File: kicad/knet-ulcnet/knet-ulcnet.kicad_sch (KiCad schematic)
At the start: 16 parts, among them U1 74LS157, U2 74LS00, U3 74LS139, U4 74LS86, U5 74LS74, U6 74LS74, U7 74LS123, U8 SN75176AP, U9 LM339

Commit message: Update schematics etc for WEB-NT product
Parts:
- added C*, C4: 103, symbol Device:C
- added C1: 10/35, symbol Device:C_Polarized
- added C2: 270p, symbol Device:C
- added C3: 470p, symbol Device:C
- added J1: EXT, symbol Connector_Generic:Conn_01x06
- added Q1: 2N2222A, symbol Device:Q_NPN_BCE
- added R10, R11: 10M, symbol Device:R
- added R12, R9: 22K, symbol Device:R
- added R2: 12K, symbol Device:R
- added R3: 47K, symbol Device:R
- added R4: 6.8K, symbol Device:R
- added R5: 120, symbol Device:R
- added R6: 3.9K1%, symbol Device:R
- added R7: 1.5K1%, symbol Device:R
- added R8: 4.7K, symbol Device:R
- ?: value SIO0-DIP-40 -> (none); Value_1 SIO0-DIP-40 -> (Z80A-SIO/0)
- D1, D2: renamed from D?; value (none) -> 5.6V
- D3, D4: renamed from D?; value D -> (none)
- J2: renamed from J?; value Conn_01x04 -> NET
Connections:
- net GND: now also U1.15 (E), U1.8 (GND), U2.7 (GND), U3.13 (A1), U3.8 (GND), U4.7 (GND), U5.7 (GND), U6.7 (GND), U7.1 (A), U7.8 (GND), U7.9 (A), U9.12 (V-), C*.2, C1.2, C4.2, J1.5 (Pin_5), Q1.3 (E), R7.2; no longer D3.2 (A), D4.2 (A), U8.5 (GND)
- net VCC: now also U1.16 (VCC), U2.13, U2.14 (VCC), U3.16 (VCC), U4.10, U4.13, U4.14 (VCC), U5.1 (~{R}), U5.10 (~{S}), U5.14 (VCC), U5.4 (~{S}), U6.1 (~{R}), U6.10 (~{S}), U6.14 (VCC), U6.4 (~{S}), U7.11 (Clr), U7.16 (VCC), U7.3 (Clr), U8.8 (VCC), U9.3 (V+), C*.1, C1.1, J1.4 (Pin_4), R2.1, R3.1, R5.2, R6.1, R8.1
- net NET: now reaches U1.1 (S), U2.10, U2.11, U3.2 (A0)
- net NET: now also U3.14 (A0)
- net 500KHz: now reaches U1.10 (I1c)
- net 500KHz: now also U4.4, U5.9 (Q)
- net 14: now reaches U1.11 (I0c)
- net /CTS: now reaches U1.12 (Zd)
- net /CTS: now also ?.18 (~{CTSA})
- net at U1.13 (I1d): now also U6.5 (Q)
- net 18: now reaches U1.14 (I0d)
- net 12: now reaches U1.2 (I0a)
- net at U1.3 (I1a): now also U4.2, U6.9 (Q)
- net RxD: now reaches U1.4 (Za)
- net RxD: now also ?.12 (RXDA)
- net 19: now reaches U1.5 (I0b)
- net /ACT: now reaches U1.6 (I1b)
- net /ACT: now also U7.12 (~{Q})
- net /DCD: now reaches U1.7 (Zb)
- net /DCD: now also ?.19 (~{DCDA})
- net TxC: now reaches U1.9 (Zc)
- net TxC: now also ?.14 (~{TXCA})
- net at D2.2 (A), U8.7 (B): now also J2.3 (Pin_3), R9.2; no longer J2.4 (Pin_4)
- net at U9.2: now also U6.2 (D), U9.13, U9.14, R10.1, R11.1, R8.2
- net VREF: now reaches U9.4 (-)
- net VREF: now also U9.10 (-), U9.8 (-), C4.1, R6.2, R7.1
- net at U9.5 (+): now also U4.8, U8.3 (DE)
- net at U3.11 (O1): now also U4.5
- net 15: now reaches U3.12 (O0)
- net TxD: now reaches U3.15 (E)
- net TxD: now also ?.15 (TXDA)
- net /NET: now reaches U2.12
- net /NET: now also ?.24 (~{RTSB}), U2.2
- net at U7.13 (Q): now also U2.9
- net at U7.14 (Cext): now also C2.2
- net at U7.15 (RCext): now also C2.1, R2.2
- net at U7.2 (B): now also U4.3
- net at U7.4 (~{Q}): now also U6.11 (C)
- net 13: now reaches U2.1
- net at U2.3: now also U2.4
- net at U4.11: now also U5.3 (C), U6.3 (C)
- net at U4.12: now also U5.11 (C), J1.6 (Pin_6)
- net at U6.12 (D): now also U4.1, U7.10 (B), U8.1 (R)
- net ACT: now reaches U7.5 (Q)
- net ACT: now also R4.1
- net at U7.6 (Cext): now also C3.2
- net at U7.7 (RCext): now also C3.1, R3.2
- net 1: now reaches ?.1 (D1)
- net 10: now reaches ?.10 (~{W}/~{RDYA})
- net RxC: now reaches ?.13 (~{RXCA})
- net RxC: now also U2.6
- net 16: now reaches ?.16 (~{DTRA})
- net 16: no longer U3.1 (E)
- net /RTS: now reaches ?.17 (~{RTSA})
- net /RTS: now also U3.1 (E)
- net 2: now reaches ?.2 (D3)
- net 20: now reaches ?.20 (Φ)
- net 21: now reaches ?.21 (~{RESET})
- net 22: now reaches ?.22 (~{DCDB})
- net 23: now reaches ?.23 (~{CTSB})
- net 25: now reaches ?.25 (~{DTRB})
- net 26: now reaches ?.26 (TXDB)
- net 27: now reaches ?.27 (~{RxTxCB})
- net 28: now reaches ?.28 (RXDB)
- net 29: now reaches ?.29 (~{SYNCB})
- net 3: now reaches ?.3 (D5)
- net 30: now reaches ?.30 (~{W}/~{RDYB})
- net 31: now reaches ?.31 (GND)
- net 32: now reaches ?.32 (~{RD})
- net 33: now reaches ?.33 (C/~{D})
- net 34: now reaches ?.34 (B/~{A})
- net 35: now reaches ?.35 (~{CE})
- net 36: now reaches ?.36 (~{IORQ})
- net 37: now reaches ?.37 (D6)
- net 38: now reaches ?.38 (D4)
- net 39: now reaches ?.39 (D2)
- net 4: now reaches ?.4 (D7)
- net 40: now reaches ?.40 (D0)
- net 5: now reaches ?.5 (~{INT})
- net 6: now reaches ?.6 (IEI)
- net 7: now reaches ?.7 (IEO)
- net 8: now reaches ?.8 (~{M1})
- net 9: now reaches ?.9 (+5V)
- net at U4.6: now also U5.2 (D)
- net at J2.2 (Pin_2): now also D3.2 (A), D4.2 (A), U8.5 (GND)
- net at D1.2 (A), U8.6 (A): now also J2.4 (Pin_4), R12.2; no longer J2.3 (Pin_3)
- net at U2.5: now also U2.8
- net at U9.11 (+): now also R10.2, R9.1
- net at U8.4 (D): now also U5.5 (Q)
- net at U9.9 (+): now also R11.2, R12.1
- net 17: now reaches U3.4 (O0)
- new net: Q1.1 (B), R4.2
- new net: J1.3 (Pin_3), Q1.2 (C)
- new net: J1.2 (Pin_2), R5.1
- no-connect marks 0 -> 12
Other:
- added sheet web-nt-cables (web-nt-cables.kicad_sch)
- note added: "(1.4V)"
- note added: "1.5uS"
- note added: "8uS"
- moved on the sheet: D1, D2, D3, D4, J2, R1, U1, U2A, U2B, U2C, U2D, U2E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

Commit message: get web-nt schematic to pass ERC
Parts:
- gave numbers to parts that had none: 1
- renumbered C* to C0
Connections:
- no-connect marks 12 -> 11
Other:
- added sheet DIP-40 (dip-40.kicad_sch)
- note added: "C0: one for each IC"
- moved on the sheet: Q1, R4

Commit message: web-nt: more analysis and disas
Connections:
- net 1MHz: now reaches J1.6 (Pin_6), U4.12, U5.11 (C)
- net /COLLISION: now reaches R10.1, R11.1, R8.2, U6.2 (D), U9.13, U9.14, U9.2
- net SEND: now reaches U4.8, U8.3 (DE), U9.5 (+)
- net /1MHz: now reaches U4.11, U5.3 (C), U6.3 (C)
- net NET-RxD: now reaches U4.1, U6.12 (D), U7.10 (B), U8.1 (R)
- net NET-TxD: now reaches U5.5 (Q), U8.4 (D)
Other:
- note added: "During transmit NET-RxD = NET-TxD unless collision"
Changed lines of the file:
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@@
+    (effects (font (size 1.27 1.27)) (justify left bottom))
+  )
+  (text "During transmit\nNET-RxD = NET-TxD\nunless collision"
+    (at 81.915 111.76 0)
     (effects (font (size 1.27 1.27)) (justify left bottom))
   )
@@
     (effects (font (size 1.27 1.27)) (justify left bottom))
   )
+  (label "NET-RxD" (at 69.85 112.395 0)
+    (effects (font (size 1.27 1.27)) (justify left bottom))
+  )
+  (label "SEND" (at 157.48 95.25 0)
+    (effects (font (size 1.27 1.27)) (justify left bottom))
+  )
   (label "TxD" (at 229.235 127.635 0)
     (effects (font (size 1.27 1.27)) (justify left bottom))
@@
     (effects (font (size 1.27 1.27)) (justify left bottom))
   )
+  (label "{slash}COLLISION" (at 82.55 64.77 0)
+    (effects (font (size 1.27 1.27)) (justify left bottom))
+  )
+  (label "1MHz" (at 144.78 40.005 90)
+    (effects (font (size 1.27 1.27)) (justify left bottom))
+  )
+  (label "NET-TxD" (at 111.76 104.775 0)
+    (effects (font (size 1.27 1.27)) (justify left bottom))
+  )
   (label "{slash}NET" (at 166.37 161.925 0)
     (effects (font (size 1.27 1.27)) (justify left bottom))
   )
+  (label "{slash}1MHz" (at 117.475 48.26 0)
+    (effects (font (size 1.27 1.27)) (justify left bottom))
+  )

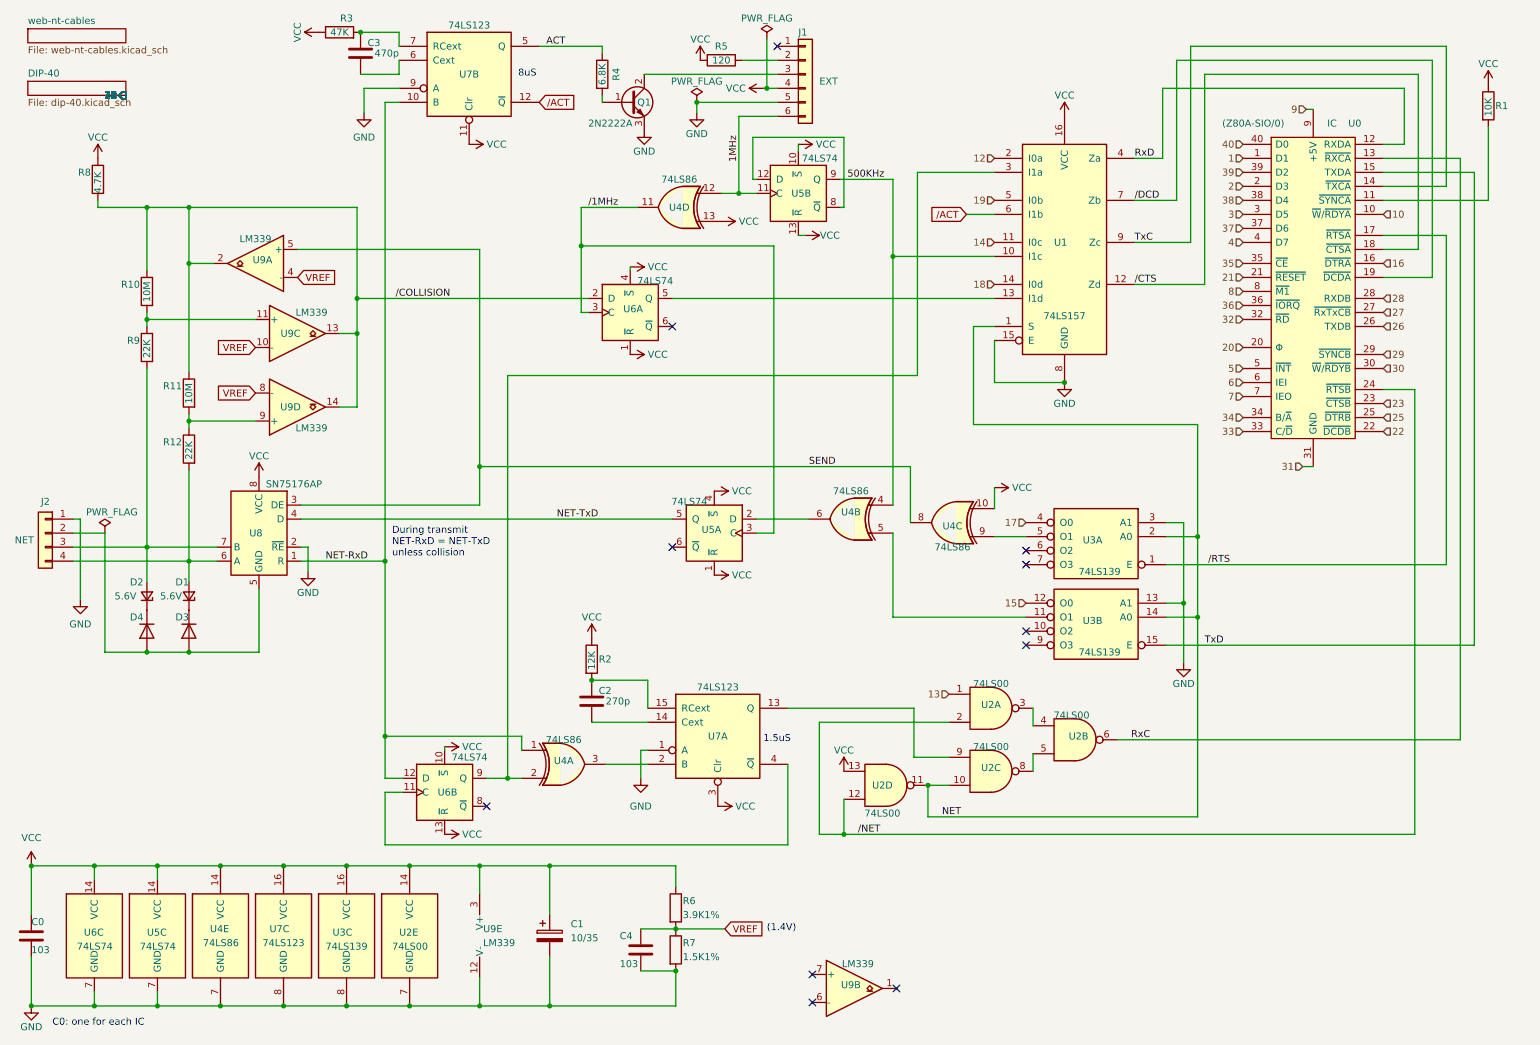
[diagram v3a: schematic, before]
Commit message: rename web-nt schematic and create possible ulcnet
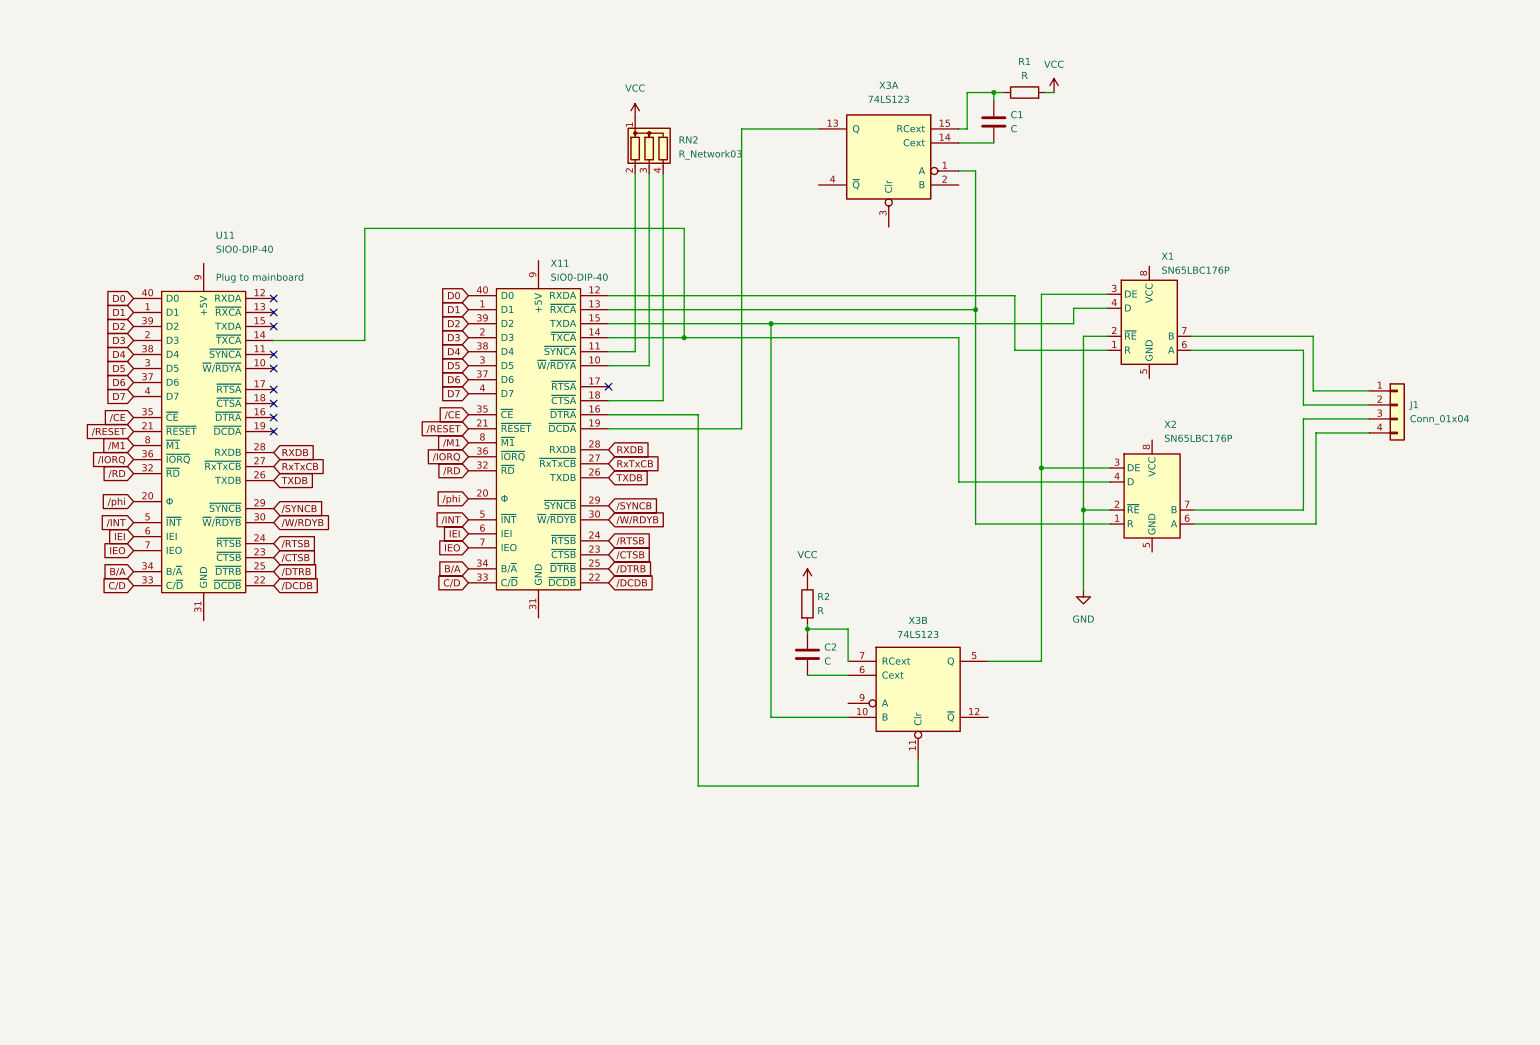
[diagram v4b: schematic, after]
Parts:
- removed C0, C4: 103, symbol Device:C
- removed C1: 10/35, symbol Device:C_Polarized
- removed C3: 470p, symbol Device:C
- removed D1, D2: 5.6V, symbol Device:D_Zener_Small
- removed D3, D4: (no value), symbol Device:D
- removed J1: EXT, symbol Connector_Generic:Conn_01x06
- removed J2: NET, symbol Connector_Generic:Conn_01x04
- removed Q1: 2N2222A, symbol Device:Q_NPN_BCE
- removed R10, R11: 10M, symbol Device:R
- removed R12, R9: 22K, symbol Device:R
- removed R3: 47K, symbol Device:R
- removed R4: 6.8K, symbol Device:R
- removed R5: 120, symbol Device:R
- removed R6: 3.9K1%, symbol Device:R
- removed R7: 1.5K1%, symbol Device:R
- removed R8: 4.7K, symbol Device:R
- removed U0: (no value), symbol Z80-peripherals:SIO0-DIP-40
- removed U1: 74LS157, symbol 74xx:74LS157
- removed U2: 74LS00, symbol 74xx:74LS00
- removed U3: 74LS139, symbol 74xx:74LS139
- removed U4: 74LS86, symbol 74xx:74LS86
- removed U5, U6: 74LS74, symbol 74xx:74LS74
- removed U7: 74LS123, symbol 74xx:74LS123
- removed U8: SN75176AP, Package_DIP:DIP-8_W7.62mm, symbol Interface_UART:SN75176AP
- removed U9: LM339, symbol Comparator:LM339
- added C1: C, symbol Device:C
- added J1: Conn_01x04, symbol Connector_Generic:Conn_01x04
- added RN2: R_Network03, Resistor_THT:R_Array_SIP4, symbol Device:R_Network03
- added U11, X11: SIO0-DIP-40, symbol Zilog_Z80_Peripherals:SIO0-DIP-40
- added X1, X2: SN65LBC176P, Package_DIP:DIP-8_W7.62mm, symbol Interface_UART:SN65LBC176P
- added X3: 74LS123, symbol 74xx:74LS123
- C2: value 270p -> C
- R1: value 10K -> R
- R2: value 12K -> R
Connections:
- net GND: now also X1.2 (~{RE}), X2.2 (~{RE})
- net VCC: now also R1.2, RN2.1 (common); no longer R1.1
- net at C2.1, R2.2: now also X3.7 (RCext)
- net at C2.2: now also X3.6 (Cext)
- new net: X11.13 (~{RXCA}), X2.1 (R), X3.1 (A)
- new net: X1.3 (DE), X2.3 (DE), X3.5 (Q)
- new net: U11.14 (~{TXCA}), X11.14 (~{TXCA}), X2.4 (D)
- new net: J1.4 (Pin_4), X2.6 (A)
- new net: J1.3 (Pin_3), X2.7 (B)
- new net: RN2.3 (R2), X11.10 (~{W}/~{RDYA})
- new net: RN2.2 (R1), X11.11 (~{SYNCA})
- new net: X1.1 (R), X11.12 (RXDA)
- new net: X1.4 (D), X11.15 (TXDA), X3.10 (B)
- new net: X11.16 (~{DTRA}), X3.11 (Clr)
- new net: RN2.4 (R3), X11.18 (~{CTSA})
- new net: X11.19 (~{DCDA}), X3.13 (Q)
- new net: C1.1, R1.1, X3.15 (RCext)
- new net: C1.2, X3.14 (Cext)
- new net: J1.1 (Pin_1), X1.7 (B)
- new net: J1.2 (Pin_2), X1.6 (A)
- new net B/A: U11.34 (B/~{A}), X11.34 (B/~{A})
- new net C/D: U11.33 (C/~{D}), X11.33 (C/~{D})
- new net D0: U11.40 (D0), X11.40 (D0)
- new net D1: U11.1 (D1), X11.1 (D1)
- new net D2: U11.39 (D2), X11.39 (D2)
- new net D3: U11.2 (D3), X11.2 (D3)
- new net D4: U11.38 (D4), X11.38 (D4)
- new net D5: U11.3 (D5), X11.3 (D5)
- new net D6: U11.37 (D6), X11.37 (D6)
- new net D7: U11.4 (D7), X11.4 (D7)
- new net IEI: U11.6 (IEI), X11.6 (IEI)
- new net IEO: U11.7 (IEO), X11.7 (IEO)
- new net RXDB: U11.28 (RXDB), X11.28 (RXDB)
- new net RxTxCB: U11.27 (~{RxTxCB}), X11.27 (~{RxTxCB})
- new net TXDB: U11.26 (TXDB), X11.26 (TXDB)
- new net /CE: U11.35 (~{CE}), X11.35 (~{CE})
- new net /CTSB: U11.23 (~{CTSB}), X11.23 (~{CTSB})
- new net /DCDB: U11.22 (~{DCDB}), X11.22 (~{DCDB})
- new net /DTRB: U11.25 (~{DTRB}), X11.25 (~{DTRB})
- new net /INT: U11.5 (~{INT}), X11.5 (~{INT})
- new net /IORQ: U11.36 (~{IORQ}), X11.36 (~{IORQ})
- new net /M1: U11.8 (~{M1}), X11.8 (~{M1})
- new net /RD: U11.32 (~{RD}), X11.32 (~{RD})
- new net /RESET: U11.21 (~{RESET}), X11.21 (~{RESET})
- new net /RTSB: U11.24 (~{RTSB}), X11.24 (~{RTSB})
- new net /SYNCB: U11.29 (~{SYNCB}), X11.29 (~{SYNCB})
- new net /W/RDYB: U11.30 (~{W}/~{RDYB}), X11.30 (~{W}/~{RDYB})
- new net /phi: U11.20 (Φ), X11.20 (Φ)
- no-connect marks 11 -> 10
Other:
- removed sheet DIP-40
- removed sheet web-nt-cables
- note removed: "(1.4V)"
- note removed: "1.5uS"
- note removed: "8uS"
- note removed: "C0: one for each IC"
- note removed: "During transmit NET-RxD = NET-TxD unless collision"
- title: (none) -> Possible KayNet-ULCNet equivalent

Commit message: working KayNetSerial, updated schematic
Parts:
- removed RN2: R_Network03, Resistor_THT:R_Array_SIP4, symbol Device:R_Network03
- removed X1, X2: SN65LBC176P, Package_DIP:DIP-8_W7.62mm, symbol Interface_UART:SN65LBC176P
- added D1: LED, symbol Device:LED
- added J1, J5: Conn_01x02_Socket, symbol Connector:Conn_01x02_Socket
- added J4, J?: Conn_01x02, symbol Connector_Generic:Conn_01x02
- added R3, R4, R5: R, symbol Device:R
- added SW1: SW_SPST, symbol Switch:SW_SPST
- added U1: MC3487N, Package_DIP:DIP-16_W7.62mm, symbol Interface_LineDriver:MC3487N
- added U2: MC3486N, Package_DIP:DIP-14_W7.62mm, symbol Interface_LineDriver:MC3486N
- added U3: 74LS06, symbol 74xx:74LS06
- added U4, U5, U6: 74LS157, symbol 74xx:74LS157
- added U9: 74LS04, symbol 74xx:74LS04
- U11: value SIO0-DIP-40 -> Mainboard
- renumbered J1 to J3
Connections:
- net GND: now also X3.10 (B), J?.2 (Pin_2), U4.15 (E), U5.15 (E), U6.15 (E)
- net VCC: now also R3.2, R4.1, R5.1, U2.4 (ENABLE), U2.4 (ENABLE)
- net at X3.1 (A): now also U2.5 (OUT), U4.6 (I1b); no longer X11.13 (~{RXCA})
- net ONLINE: now reaches X3.5 (Q)
- net ONLINE: now also U1.4 (ENABLE), U1.4 (ENABLE), U4.1 (S)
- net at U11.14 (~{TXCA}), X11.14 (~{TXCA}): now also U1.7 (INPUT), U4.5 (I0b)
- net +CLK: now reaches J3.4 (Pin_4)
- net +CLK: now also U1.6 (OUT+), U2.6 (E+)
- net -CLK: now reaches J3.3 (Pin_3)
- net -CLK: now also U1.5 (OUT-), U2.7 (E-)
- net M-/W/RDYA: now reaches X11.10 (~{W}/~{RDYA})
- net M-/W/RDYA: now also U11.10 (~{W}/~{RDYA})
- net M-/SYNCA: now reaches X11.11 (~{SYNCA})
- net M-/SYNCA: now also U11.11 (~{SYNCA})
- net at X11.12 (RXDA): now also U5.4 (Za)
- net at X11.15 (TXDA): now also U5.10 (I1c), U6.14 (I0d); no longer X3.10 (B)
- net at X11.16 (~{DTRA}): now also U6.10 (I1c), U6.5 (I0b); no longer X3.11 (Clr)
- net at X11.17 (~{RTSA}): now also U6.2 (I0a)
- net M-/CTSA: now reaches X11.18 (~{CTSA})
- net M-/CTSA: now also U11.18 (~{CTSA})
- net at X11.19 (~{DCDA}): now also U5.12 (Zd); no longer X3.13 (Q)
- net N-TxDA: now reaches X3.9 (A)
- net N-TxDA: now also U1.1 (INPUT), U4.2 (I0a), U5.9 (Zc)
- net /ACTIVE: now reaches X3.4 (~{Q})
- net /ACTIVE: now also U3.1
- net -DAT: now reaches J3.1 (Pin_1)
- net -DAT: now also U1.3 (OUT-), U2.1 (E-)
- net +DAT: now reaches J3.2 (Pin_2)
- net +DAT: now also U1.2 (OUT+), U2.2 (E+)
- net M-RxDA: now reaches U11.12 (RXDA)
- net M-RxDA: now also U5.2 (I0a)
- net M-/RxCA: now reaches U11.13 (~{RXCA})
- net M-/RxCA: now also U5.5 (I0b)
- net M-TxDA: now reaches U11.15 (TXDA)
- net M-TxDA: now also U6.12 (Zd)
- net M-/DTRA: now reaches U11.16 (~{DTRA})
- net M-/DTRA: now also U6.7 (Zb)
- net M-/RTSA: now reaches U11.17 (~{RTSA})
- net M-/RTSA: now also U6.4 (Za)
- net M-/DCDA: now reaches U11.19 (~{DCDA})
- net M-/DCDA: now also U5.14 (I0d)
- net RXDB renamed RxDB
- net RxTxCB renamed /RxTxCB
- net TXDB renamed TxDB
- new net: U2.3 (OUT), U4.3 (I1a)
- new net: U5.7 (Zb), X11.13 (~{RXCA})
- new net: U9.2, X3.11 (Clr)
- new net: D1.1 (K), J1.2 (Pin_2)
- new net: D1.2 (A), J1.1 (Pin_1)
- new net: J5.1 (Pin_1), SW1.1 (A)
- new net: J5.2 (Pin_2), SW1.2 (B)
- new net: J?.1 (Pin_1), R4.2, U9.3
- new net: J4.1 (Pin_1), R3.1
- new net: J4.2 (Pin_2), U3.2
- new net ACTIVE: U5.13 (I1d), X3.13 (Q)
- new net N-RxDA: U4.4 (Za), U5.3 (I1a)
- new net N-/DTR: U6.9 (Zc), U9.1
- new net N-/RxCA: U4.7 (Zb), U5.6 (I1b)
- new net NET: U5.1 (S), U6.1 (S), U9.4
- new net P.U.: R5.2, U5.11 (I0c), U6.11 (I0c), U6.13 (I1d), U6.3 (I1a), U6.6 (I1b)
- no-connect marks 10 -> 0
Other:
- note added: "Mentioned In Manual Details Unknown"
- note added: "On Rear Panel"
- note added: "POWER LED on front panel"
- moved on the sheet: C2, J3, R2, X11, X3B
